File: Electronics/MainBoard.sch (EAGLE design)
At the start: 10 parts, among them J1 1X2-3.5MM

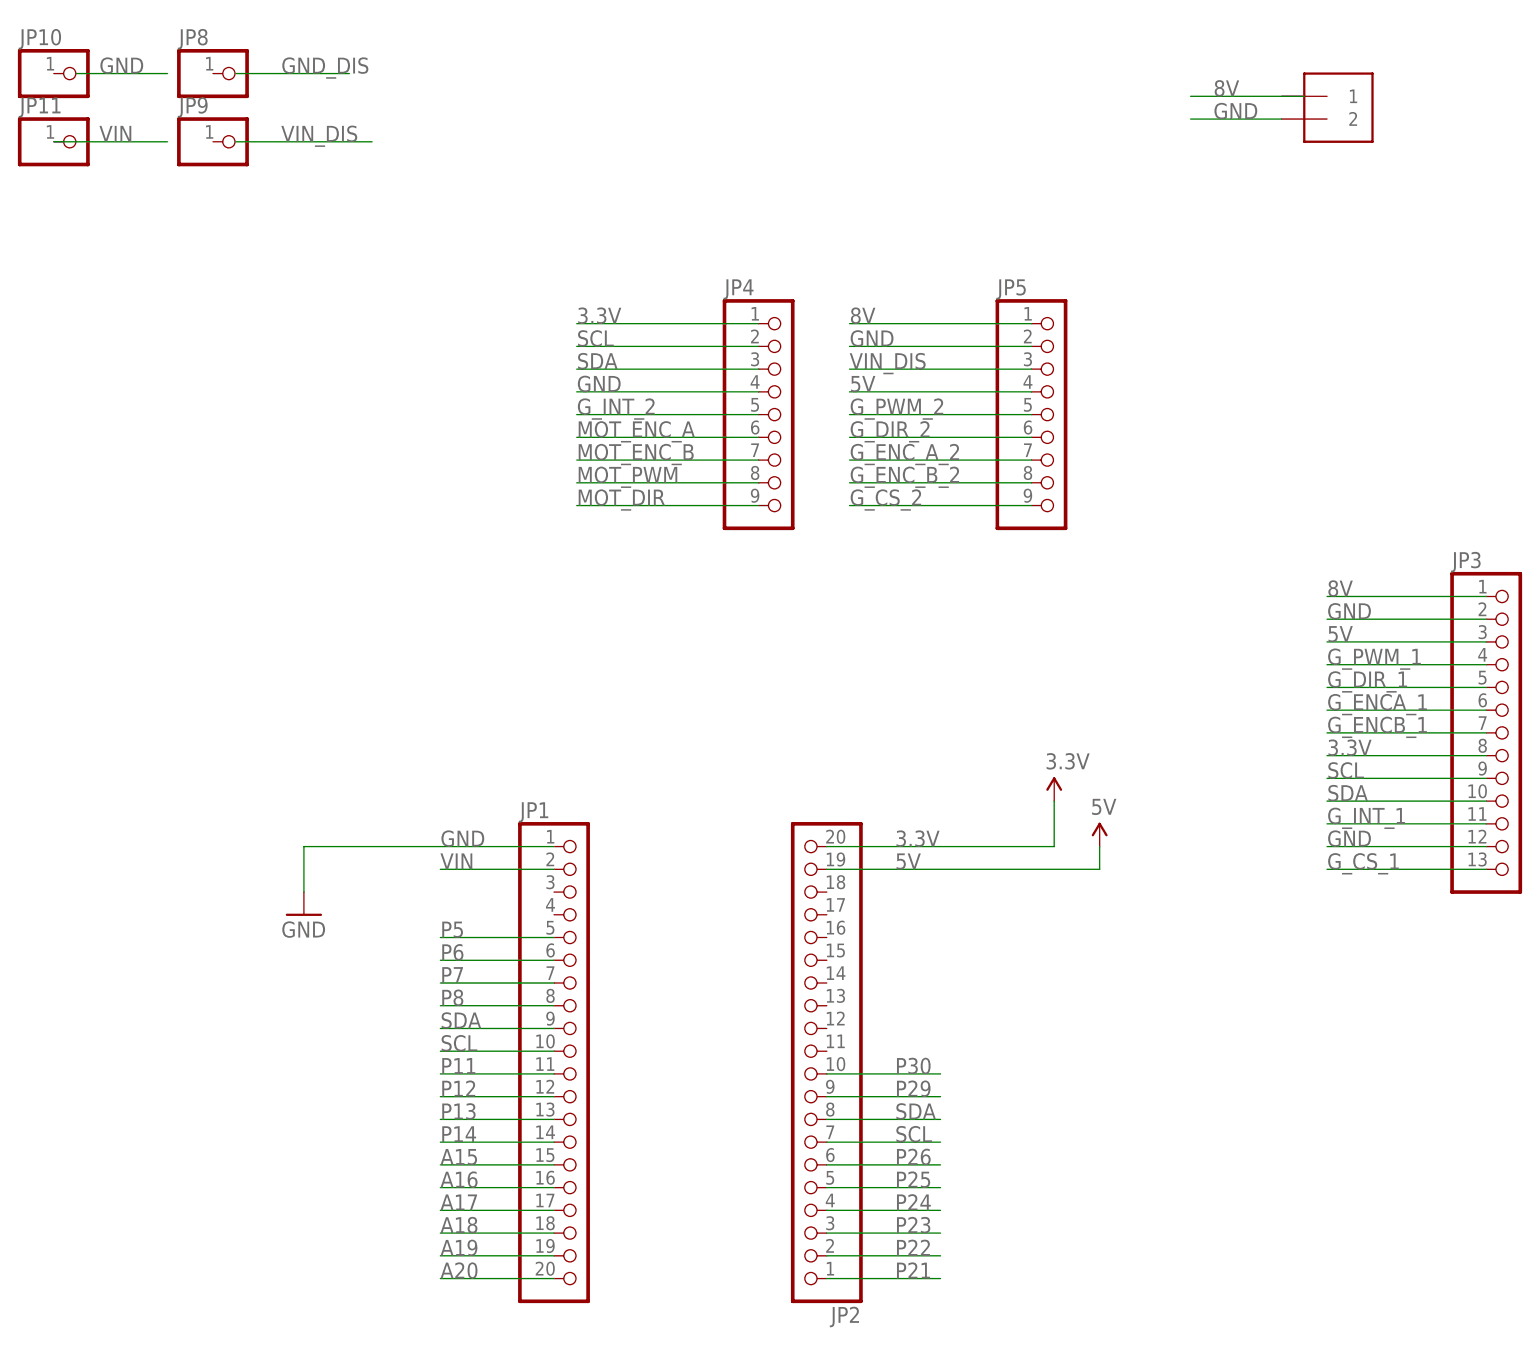
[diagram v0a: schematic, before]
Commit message: power routed
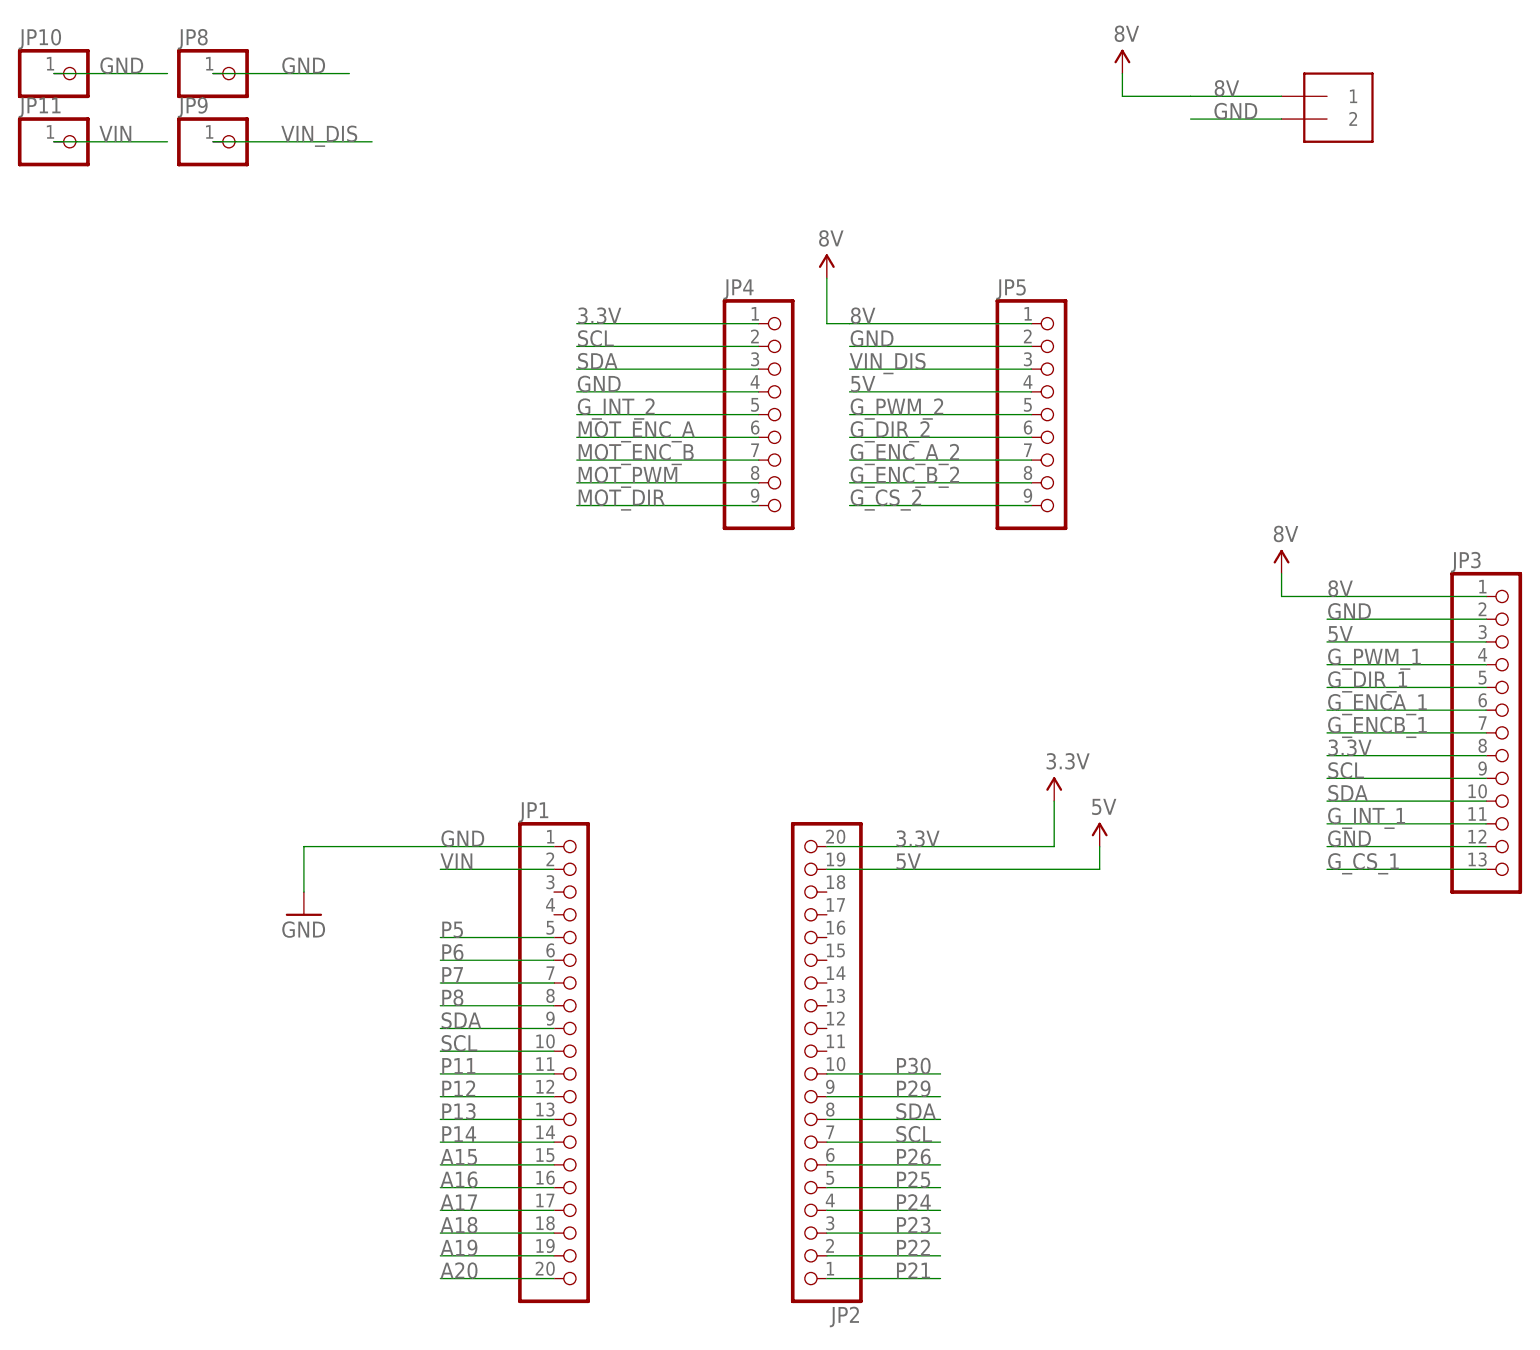
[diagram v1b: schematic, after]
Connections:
- net 8V: now also J1.1
- net GND: now also JP10.1, JP8.1
- net VIN_DIS: now also JP9.1
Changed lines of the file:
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@@
 <part name="JP11" library="adafruit" deviceset="PINHD-1X1" device=""/>
 <part name="J1" library="adafruit" deviceset="1X2" device="-3.5MM"/>
+<part name="8V" library="SparkFun" deviceset="VCC" device="" value="8V"/>
+<part name="8V1" library="SparkFun" deviceset="VCC" device="" value="8V"/>
+<part name="8V2" library="SparkFun" deviceset="VCC" device="" value="8V"/>
 </parts>
 <sheets>
@@
 <instance part="JP11" gate="G$1" x="-38.1" y="185.42"/>
 <instance part="J1" gate="G$1" x="101.6" y="187.96"/>
+<instance part="8V" gate="1" x="96.52" y="137.16"/>
+<instance part="8V1" gate="1" x="78.74" y="193.04"/>
+<instance part="8V2" gate="1" x="45.72" y="170.18"/>
 </instances>
 <busses>
@@
 <wire x1="-38.1" y1="193.04" x2="-27.94" y2="193.04" width="0.1524" layer="91"/>
 <label x="-35.56" y="193.04" size="1.778" layer="95"/>
+<pinref part="JP10" gate="G$1" pin="1"/>
+<wire x1="-38.1" y1="193.04" x2="-40.64" y2="193.04" width="0.1524" layer="91"/>
 </segment>
 <segment>
@@
 <wire x1="96.52" y1="187.96" x2="86.36" y2="187.96" width="0.1524" layer="91"/>
 <label x="88.9" y="187.96" size="1.778" layer="95"/>
+</segment>
+<segment>
+<wire x1="-20.32" y1="193.04" x2="-7.62" y2="193.04" width="0.1524" layer="91"/>
+<label x="-15.24" y="193.04" size="1.778" layer="95"/>
+<pinref part="JP8" gate="G$1" pin="1"/>
+<wire x1="-20.32" y1="193.04" x2="-22.86" y2="193.04" width="0.1524" layer="91"/>
 </segment>
 </net>
@@
 <wire x1="119.38" y1="134.62" x2="101.6" y2="134.62" width="0.1524" layer="91"/>
 <label x="101.6" y="134.62" size="1.778" layer="95"/>
+<pinref part="8V" gate="1" pin="VCC"/>
+<wire x1="101.6" y1="134.62" x2="96.52" y2="134.62" width="0.1524" layer="91"/>
+<wire x1="96.52" y1="134.62" x2="96.52" y2="137.16" width="0.1524" layer="91"/>
+</segment>
+<segment>
+<label x="88.9" y="190.5" size="1.778" layer="95"/>
+<pinref part="8V1" gate="1" pin="VCC"/>
+<wire x1="86.36" y1="190.5" x2="78.74" y2="190.5" width="0.1524" layer="91"/>
+<wire x1="78.74" y1="190.5" x2="78.74" y2="193.04" width="0.1524" layer="91"/>
+<pinref part="J1" gate="G$1" pin="1"/>
+<wire x1="86.36" y1="190.5" x2="96.52" y2="190.5" width="0.1524" layer="91"/>
 </segment>
 <segment>
@@
 <wire x1="68.58" y1="165.1" x2="48.26" y2="165.1" width="0.1524" layer="91"/>
 <label x="48.26" y="165.1" size="1.778" layer="95"/>
-</segment>
-<segment>
-<wire x1="99.06" y1="190.5" x2="86.36" y2="190.5" width="0.1524" layer="91"/>
-<label x="88.9" y="190.5" size="1.778" layer="95"/>
+<pinref part="8V2" gate="1" pin="VCC"/>
+<wire x1="48.26" y1="165.1" x2="45.72" y2="165.1" width="0.1524" layer="91"/>
+<wire x1="45.72" y1="165.1" x2="45.72" y2="170.18" width="0.1524" layer="91"/>
 </segment>
 </net>
@@
 </segment>
 <segment>
+<wire x1="-38.1" y1="185.42" x2="-27.94" y2="185.42" width="0.1524" layer="91"/>
+<label x="-35.56" y="185.42" size="1.778" layer="95"/>
 <pinref part="JP11" gate="G$1" pin="1"/>
-<wire x1="-40.64" y1="185.42" x2="-27.94" y2="185.42" width="0.1524" layer="91"/>
-<label x="-35.56" y="185.42" size="1.778" layer="95"/>
+<wire x1="-38.1" y1="185.42" x2="-40.64" y2="185.42" width="0.1524" layer="91"/>
 </segment>
 </net>
@@
 <wire x1="-20.32" y1="185.42" x2="-5.08" y2="185.42" width="0.1524" layer="91"/>
 <label x="-15.24" y="185.42" size="1.778" layer="95"/>
-</segment>
-</net>
-<net name="GND_DIS" class="0">
-<segment>
-<wire x1="-20.32" y1="193.04" x2="-7.62" y2="193.04" width="0.1524" layer="91"/>
-<label x="-15.24" y="193.04" size="1.778" layer="95"/>
-</segment>
-</net>
+<pinref part="JP9" gate="G$1" pin="1"/>
+<wire x1="-20.32" y1="185.42" x2="-22.86" y2="185.42" width="0.1524" layer="91"/>
+</segment>
+</net>
